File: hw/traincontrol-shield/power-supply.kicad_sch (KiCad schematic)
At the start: 10 parts, among them U1 MP2359DJ

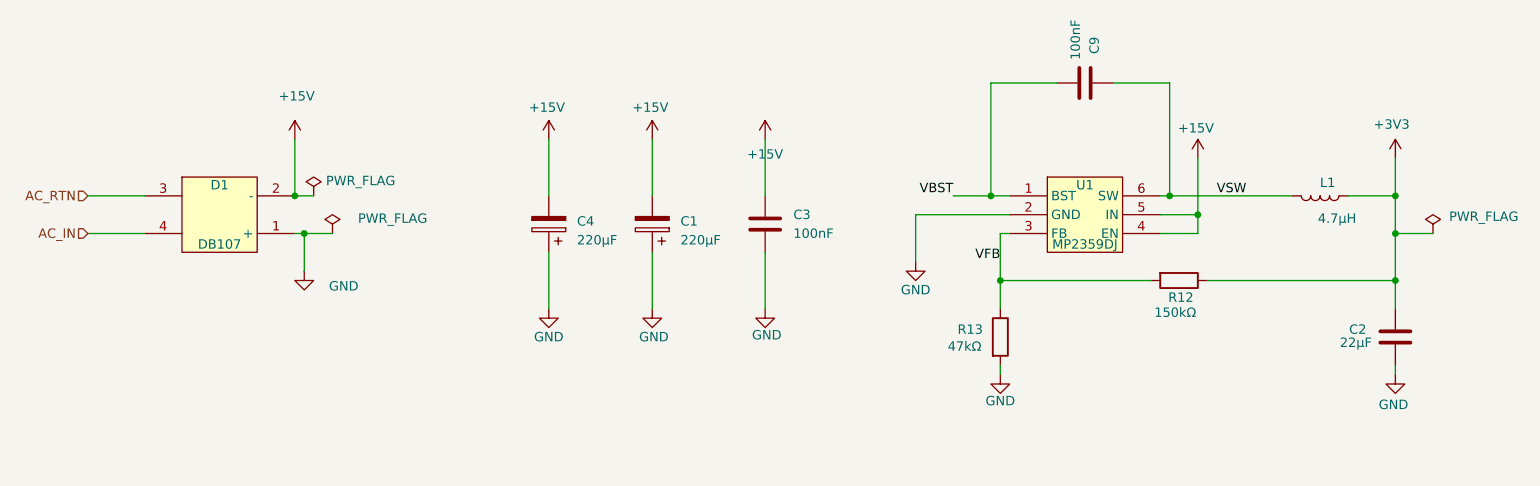
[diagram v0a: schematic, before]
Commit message: Update BOM, docs, and JLCPCB outputs to match current schematics
- Update BOM.md with JLCPCB LCSC part numbers for all components
- Generate JLCPCB BOM and CPL files for PCBA ordering
- Update docs and README to reflect component changes (BAT54S/SS34
  rectification, BT134W-600E TRIACs, EL357N optocoupler, ESP32-C3)
- Suppress ERC warnings for unspecified pin connections in project settings

Co-Authored-By: Claude Opus 4.6 <noreply@anthropic.com>
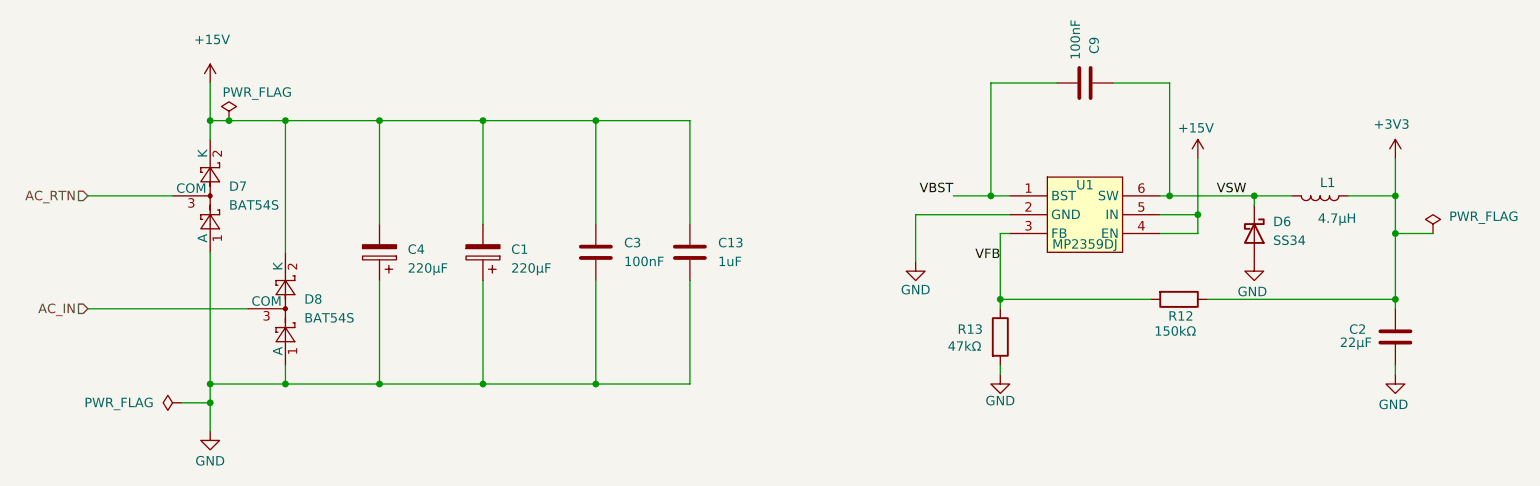
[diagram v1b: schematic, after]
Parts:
- removed D1: DB107, traincontrol-shield:DIO-BG-TH_DF, symbol traincontrol-shield:DB107
- added C13: 1uF, Capacitor_SMD:C_0603_1608Metric, symbol Device:C
- added D6: SS34, Diode_SMD:D_SMA, symbol Diode:SS34
- added D7, D8: BAT54S, Package_TO_SOT_SMD:SOT-23, symbol Diode:BAT54S
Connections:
- net +15V: now also C13.2, D7.2 (K), D8.2 (K)
- net AC_IN: now also D8.3 (COM)
- net AC_RTN: now also D7.3 (COM)
- net GND: now also C13.1, D6.2 (A), D7.1 (A), D8.1 (A)
- net VSW: now also D6.1 (K)
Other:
- moved on the sheet: C1, C3, C4, R12
